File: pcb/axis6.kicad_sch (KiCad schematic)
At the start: 7 parts, among them J16 Mini v1.0 / 15-hole socket, J26 MOTOR PHASES male 1x3, J36 ENCODER breakout FEMALE 1x6

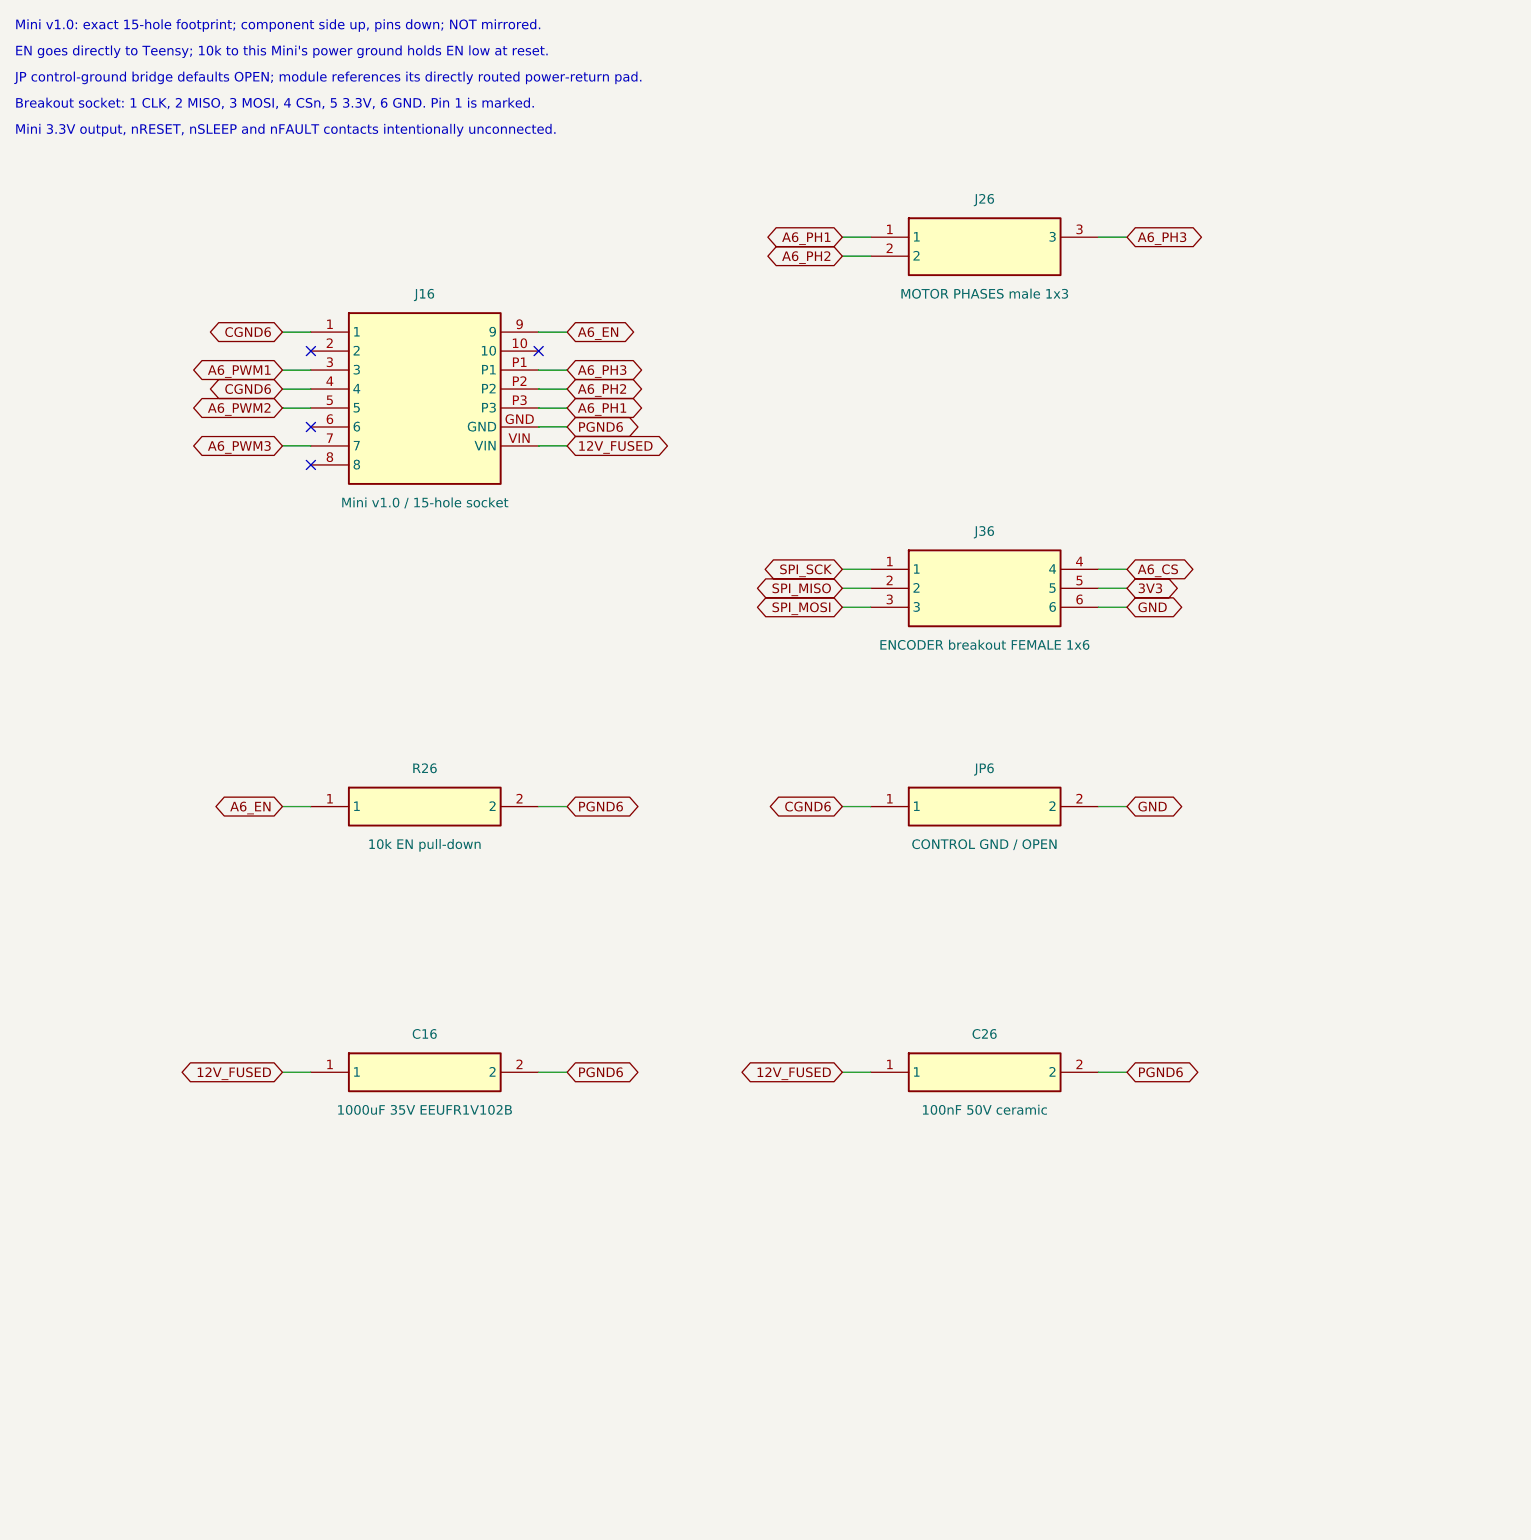
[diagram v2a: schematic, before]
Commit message: feat: relayout carrier with edge connectors and hardware kill
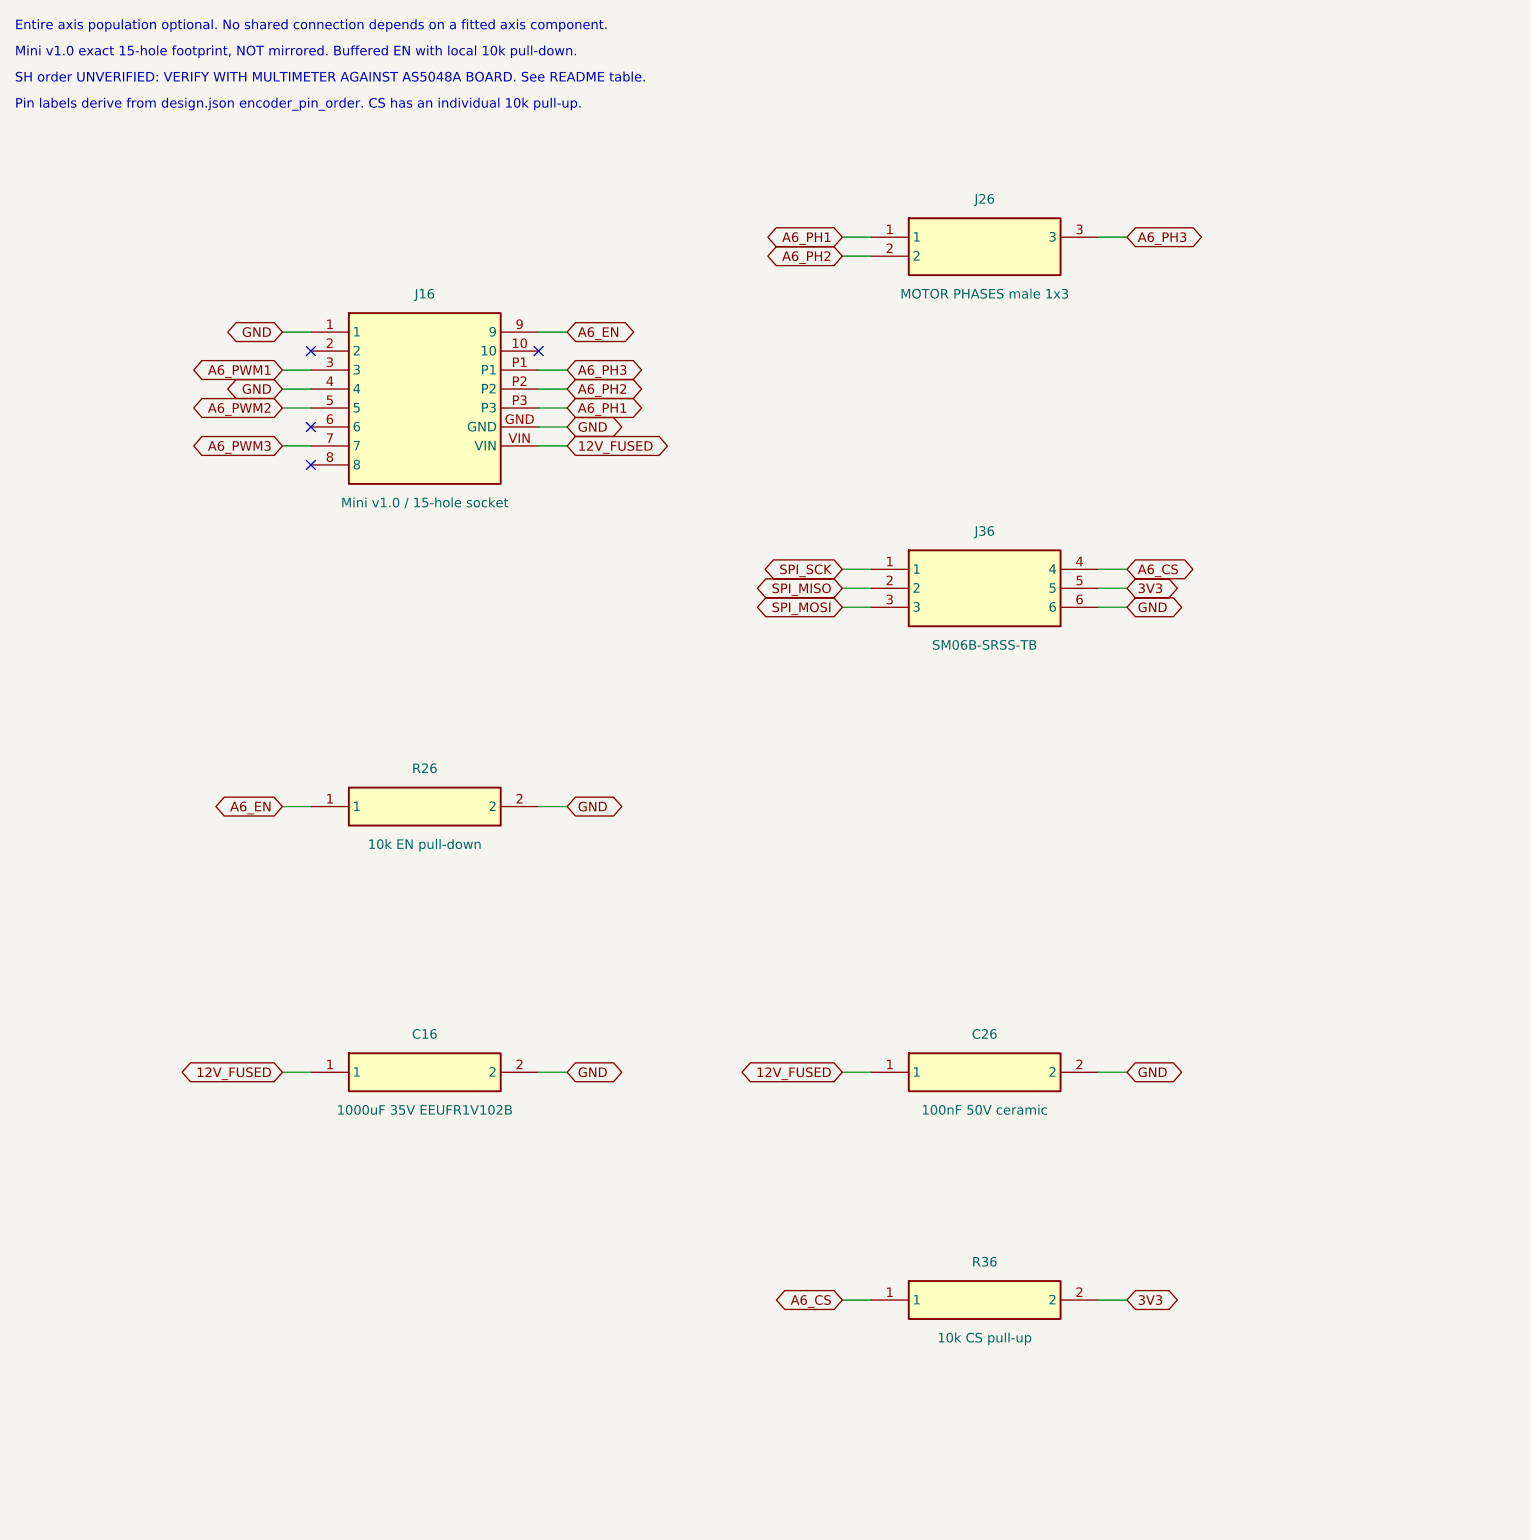
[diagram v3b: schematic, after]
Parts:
- removed JP6: CONTROL GND / OPEN, TrueSkate:GroundBridge_THT, symbol TrueSkate:JP6
- added R36: 10k CS pull-up, TrueSkate:Edge_R_Axial_DIN0207_L6.3mm_D2.5mm_P7.62mm_Horizontal, symbol TrueSkate:R36
- C16: footprint Capacitor_THT:CP_Radial_D12.5mm_P5.00mm -> TrueSkate:Edge_CP_Radial_D12.5mm_P5.00mm
- C26: footprint Capacitor_THT:C_Disc_D5.0mm_W2.5mm_P5.00mm -> TrueSkate:Edge_C_Disc_D5.0mm_W2.5mm_P5.00mm
- J26: footprint Connector_PinHeader_2.54mm:PinHeader_1x03_P2.54mm_Vertical -> TrueSkate:Edge_PinHeader_1x03_P2.54mm_Vertical
- J36: value ENCODER breakout FEMALE 1x6 -> SM06B-SRSS-TB; footprint Connector_PinSocket_2.54mm:PinSocket_1x06_P2.54mm_Vertical -> TrueSkate:Edge_JST_SH_SM06B-SRSS-TB_1x06-1MP_P1.00mm_Horizontal
- R26: footprint Resistor_THT:R_Axial_DIN0207_L6.3mm_D2.5mm_P7.62mm_Horizontal -> TrueSkate:Edge_R_Axial_DIN0207_L6.3mm_D2.5mm_P7.62mm_Horizontal
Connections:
- net CGND6 is gone; now on net GND: J16.1, J16.4
- net PGND6 is gone; now on net GND: C16.2, C26.2, J16.GND, R26.2
- net 3V3: now also R36.2
- net A6_CS: now also R36.1
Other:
- note added: "Entire axis population optional. No shared connection depends on a fitted axis component."
- note added: "Mini v1.0 exact 15-hole footprint, NOT mirrored. Buffered EN with local 10k pull-down."
- note added: "Pin labels derive from design.json encoder_pin_order. CS has an individual 10k pull-up."
- note added: "SH order UNVERIFIED: VERIFY WITH MULTIMETER AGAINST AS5048A BOARD. See README table."
- note removed: "Breakout socket: 1 CLK, 2 MISO, 3 MOSI, 4 CSn, 5 3.3V, 6 GND. Pin 1 is marked."
- note removed: "EN goes directly to Teensy; 10k to this Mini's power ground holds EN low at reset."
- note removed: "JP control-ground bridge defaults OPEN; module references its directly routed power-return pad."
- note removed: "Mini 3.3V output, nRESET, nSLEEP and nFAULT contacts intentionally unconnected."
- note removed: "Mini v1.0: exact 15-hole footprint; component side up, pins down; NOT mirrored."
